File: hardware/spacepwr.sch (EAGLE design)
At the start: 7 parts, among them IC1 MEGA32-P, IC2 UDN2981A, IC3 UDN2981A, IC4 LM2596T, IC5 MEGA8-P

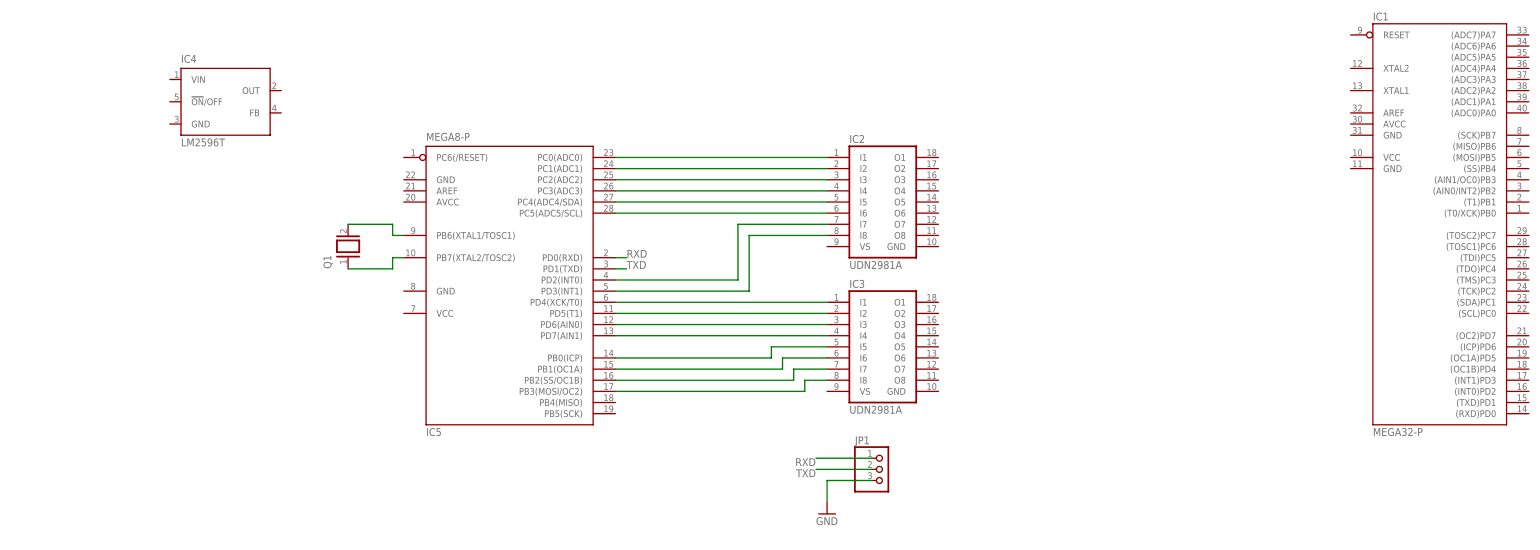
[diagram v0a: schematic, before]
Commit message: added screw terminals
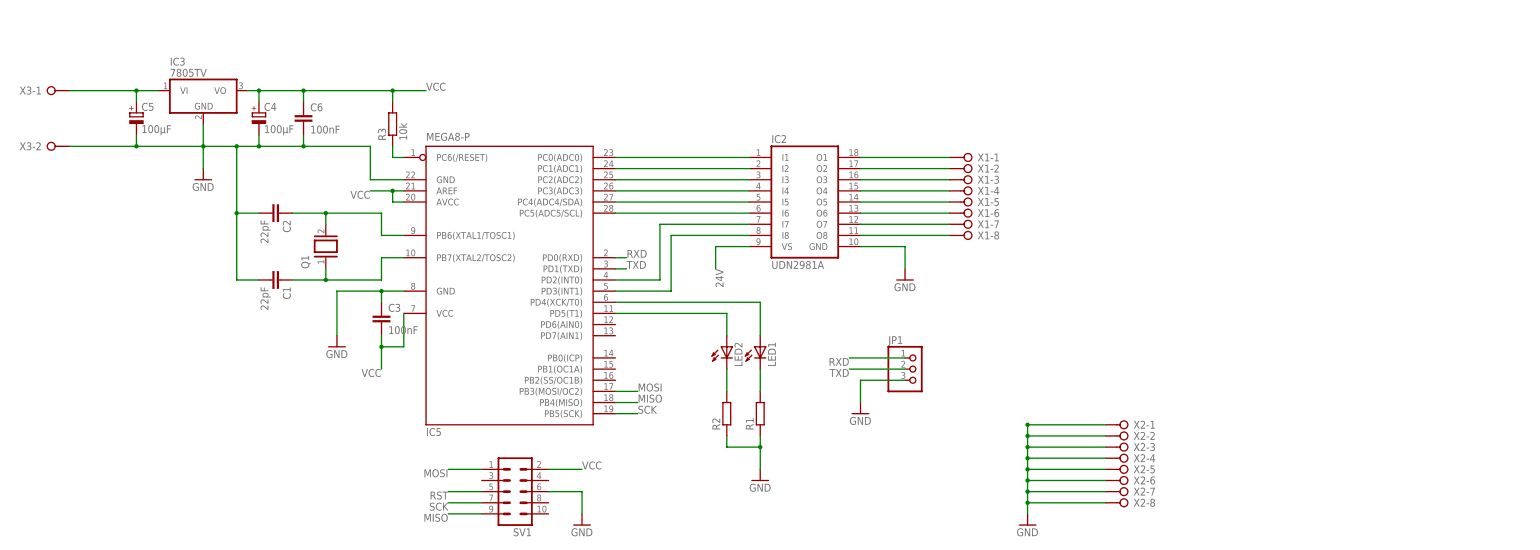
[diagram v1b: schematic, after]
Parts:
- removed IC1: MEGA32-P, atmel:MEGA32-P
- removed IC4: LM2596T, national-semiconductor:LM2596T
- added C1, C2: 22pF, rcl:C-EU025-030X050
- added C3, C6: 100nF, rcl:C-EU025-030X050
- added C4, C5: 100µF, rcl:CPOL-EUE5-10.5
- added LED1, LED2: (no value), led:LED5MM
- added R1, R2: (no value), rcl:R-EU_0207/10
- added R3: 10k, rcl:R-EU_0207/10
- added SV1: (no value), con-ml:ML10
- added X1, X2: (no value), con-wago-508:W237-08P
- added X3: (no value), con-wago-508:W237-02P
- IC3: value UDN2981A -> 7805TV; device uln-udn:UDN2981A -> linear:7805TV
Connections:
- new net 24V: C5.+, IC2.VS, IC3.VI, X3-1.KL
- new net MISO: IC5.PB4(MISO), SV1.9
- new net MOSI: IC5.PB3(MOSI/OC2), SV1.1
- new net N$19: IC2.O5, X1-5.KL
- new net N$20: IC2.O6, X1-6.KL
- new net N$21: IC2.O7, X1-7.KL
- new net N$22: IC2.O8, X1-8.KL
- new net RST: IC5.PC6(/RESET), R3.1, SV1.5
- new net SCK: IC5.PB5(SCK), SV1.7
- new net VCC: C3.2, C4.+, C6.1, IC3.VO, IC5.AREF, IC5.AVCC, IC5.VCC@1, R3.2, SV1.2
- net GND: now also C1.2, C2.2, C3.1, C4.-, C5.-, C6.2, IC2.GND, IC3.GND, IC5.GND, IC5.GND@1, R1.1, R2.1, SV1.6, X2-1.KL, X2-2.KL, X2-3.KL, X2-4.KL, X2-5.KL, X2-6.KL, X2-7.KL, X2-8.KL, X3-2.KL
- net N$10: now also IC5.PD4(XCK/T0), LED1.A; no longer IC3.I2, IC5.PD5(T1)
- net N$11: now also IC2.O1, X1-1.KL; no longer IC3.I3, IC5.PD6(AIN0)
- net N$12: now also IC5.PD5(T1), LED2.A; no longer IC3.I4, IC5.PD7(AIN1)
- net N$13: now also LED2.C, R2.2; no longer IC3.I5, IC5.PB0(ICP)
- net N$14: now also IC2.O2, X1-2.KL; no longer IC3.I6, IC5.PB1(OC1A)
- net N$15: now also IC2.O3, X1-3.KL; no longer IC3.I7, IC5.PB2(SS/OC1B)
- net N$16: now also IC2.O4, X1-4.KL; no longer IC3.I8, IC5.PB3(MOSI/OC2)
- net N$17: now also C1.1, IC5.PB7(XTAL2/TOSC2), Q1.1; no longer IC5.PB6(XTAL1/TOSC1), Q1.2
- net N$18: now also C2.1, IC5.PB6(XTAL1/TOSC1), Q1.2; no longer IC5.PB7(XTAL2/TOSC2), Q1.1
- net N$9: now also LED1.C, R1.2; no longer IC3.I1, IC5.PD4(XCK/T0)
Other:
- moved on the sheet: IC2, JP1, Q1
